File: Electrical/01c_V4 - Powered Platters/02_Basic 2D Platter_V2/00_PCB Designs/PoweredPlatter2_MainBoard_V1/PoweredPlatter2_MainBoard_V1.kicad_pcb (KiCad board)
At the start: 2 copper layers, 60 x 60 mm, 24 parts, among them J1 Conn_01x08, J2 Conn_01x08, J3 M20-7920242R, J4 Conn_01x03, U1 STM32C071KBTx, Y1 16Mhz, 3.2 x 2.5

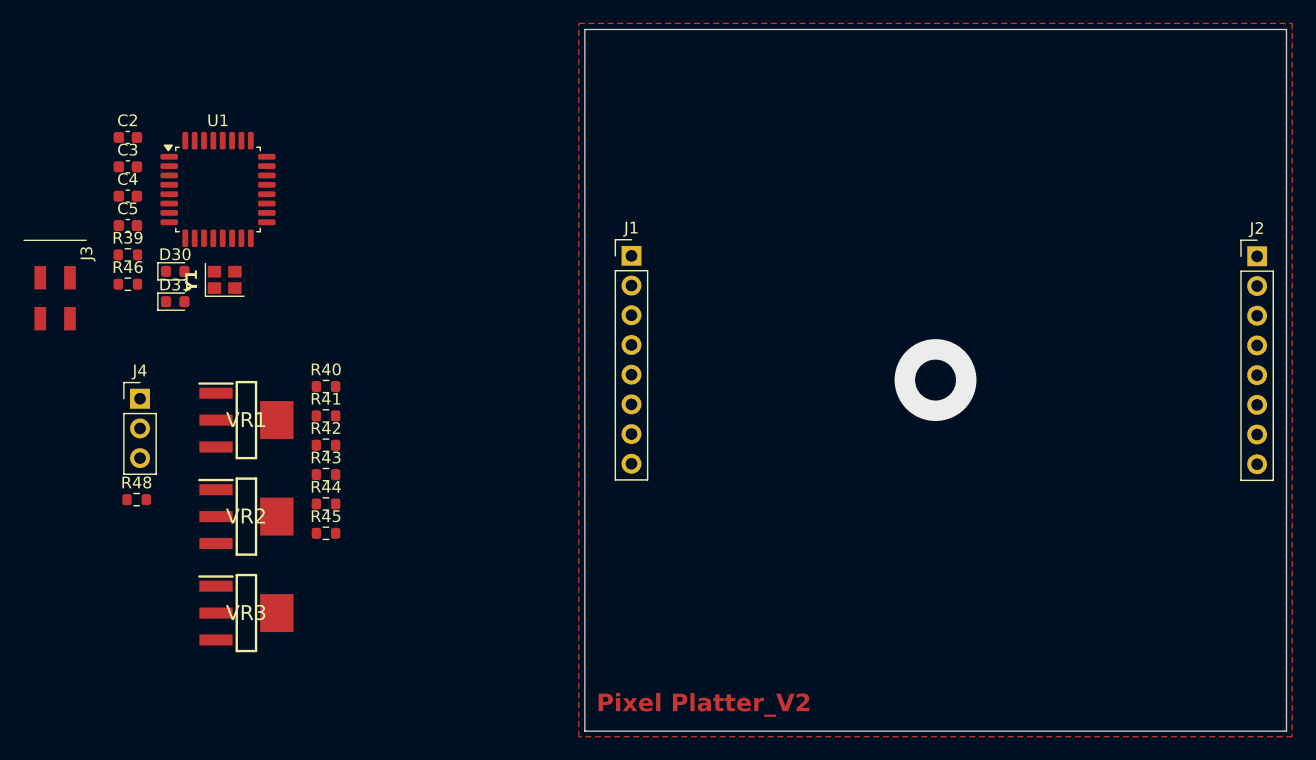
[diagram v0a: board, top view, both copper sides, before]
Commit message: second powered platter main PCB designed and ready for CNC milling
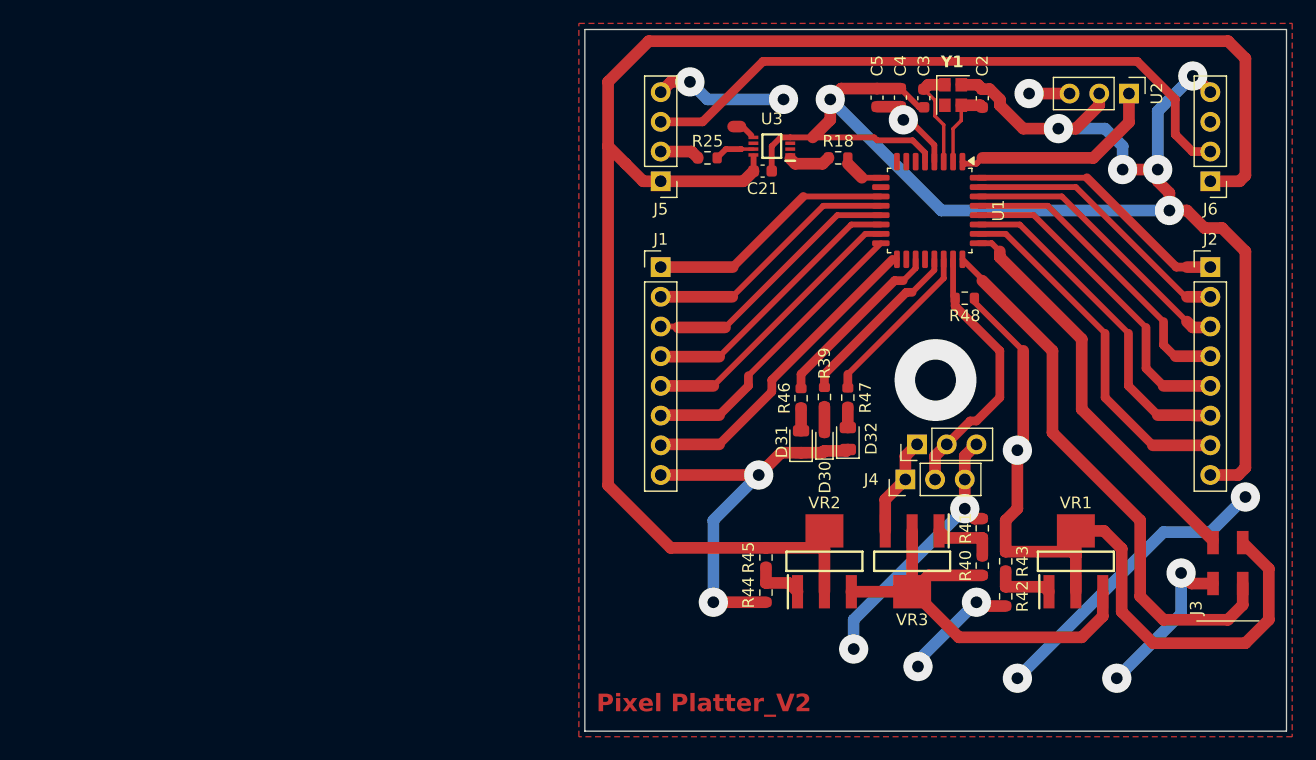
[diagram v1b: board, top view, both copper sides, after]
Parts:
- added C21: 0.1uF_0603, Capacitor_SMD:C_0603_1608Metric, F.Cu at (127.2, 72.1)
- added D32: LED_0805_GREEN, LED_SMD:LED_0805_2012Metric, F.Cu at (134.5, 95.0)
- added J5: Conn_01x04, Connector_PinHeader_2.54mm:PinHeader_1x04_P2.54mm_Vertical, F.Cu at (118.5, 73.0)
- added J5: Conn_01x03, Connector_PinHeader_2.54mm:PinHeader_1x03_P2.54mm_Vertical, F.Cu at (140.4, 95.5)
- added J6: Conn_01x04, Connector_PinHeader_2.54mm:PinHeader_1x04_P2.54mm_Vertical, F.Cu at (165.5, 73.0)
- added R18: 300ohm_0603, Resistor_SMD:R_0603_1608Metric, F.Cu at (133.7, 71.0)
- added R25: 300ohm_0603, Resistor_SMD:R_0603_1608Metric, F.Cu at (122.5, 71.0)
- added R47: 1kohm_0603, Resistor_SMD:R_0603_1608Metric, F.Cu at (134.5, 91.5)
- added U2: IR_Receiver, Connector_PinHeader_2.54mm:PinHeader_1x03_P2.54mm_Vertical, F.Cu at (158.5, 65.5)
- added U3: 74HC3G34DC, PixelPlatter:74HC3G34DC, F.Cu at (128.0, 70.0)
- D31: value LED_0603_BLUE -> LED_0805_RED; footprint LED_SMD:LED_0603_1608Metric -> LED_SMD:LED_0805_2012Metric
- moved J3 106.0 mm to (167.0, 111.5), turned to 180 degrees
- moved C2 73.1 mm to (146.0, 65.9), turned to 90 degrees
- moved R48 72.9 mm to (144.5, 83.0)
- moved VR1 72.0 mm to (154.0, 105.5), turned to 90 degrees
- moved C3 68.3 mm to (141.0, 65.9), turned to 90 degrees
- moved C4 66.6 mm to (139.0, 65.8), turned to 90 degrees
- moved J4 65.8 mm to (139.4, 98.5), turned to 90 degrees
- moved C5 65.0 mm to (137.0, 65.8), turned to 90 degrees
- moved Y1 64.3 mm to (143.5, 65.6), turned to -90 degrees
- moved U1 60.9 mm to (141.5, 75.5), turned to -90 degrees
- moved R39 60.8 mm to (132.5, 91.5), turned to 90 degrees
- moved R42 59.5 mm to (148.0, 108.5), turned to -90 degrees
- moved R43 58.6 mm to (148.0, 105.5), turned to -90 degrees
- moved R46 58.4 mm to (130.5, 91.5), turned to 90 degrees
- moved R40 58.2 mm to (146.0, 105.9), turned to 90 degrees
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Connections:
- J2 pad 1: bladeLED8 -> bladeLED14
- J2 pad 2: bladeLED9 -> bladeLED13
- J2 pad 3: bladeLED10 -> bladeLED12
- J2 pad 5: bladeLED12 -> bladeLED10
- J2 pad 6: bladeLED13 -> bladeLED9
- J2 pad 7: bladeLED14 -> bladeLED8
- U1 pad 1: unconnected-(U1-PB9-Pad1) -> IR_input
- U1 pad 10: bladeLED4 -> unconnected-(U1-PA3-Pad10)
- U1 pad 11: bladeLED5 -> bladeLED1
- U1 pad 12: bladeLED6 -> bladeLED2
- U1 pad 13: bladeLED7 -> bladeLED3
- U1 pad 14: unconnected-(U1-PA7-Pad14) -> bladeLED4
- U1 pad 15: unconnected-(U1-PB0-Pad15) -> bladeLED5
- U1 pad 16: unconnected-(U1-PB1-Pad16) -> bladeLED6
- U1 pad 17: unconnected-(U1-PB2-Pad17) -> bladeLED7
- U1 pad 19: unconnected-(U1-PA9-Pad19) -> testLED2
- U1 pad 21: unconnected-(U1-PA10-Pad21) -> testLED
- U1 pad 22: testLED2 -> testLED3
- U1 pad 23: testLED -> strobe
- U1 pad 7: bladeLED1 -> unconnected-(U1-PA0-Pad7)
- U1 pad 8: bladeLED2 -> unconnected-(U1-PA1-Pad8)
- U1 pad 9: bladeLED3 -> neopixels_3v3
- Y1 pad 2: GND -> unconnected-(Y1-Pad2)
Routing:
- net GND: track 0.00 -> 254.9 mm, vias 1 -> 18
- net +5V: track 0.00 -> 145.6 mm
- net +3V3: track 0.00 -> 121.6 mm, vias 0 -> 3
- net /Connectors/neopixelOutIn: track 0.00 -> 54.1 mm
- net SWDIO: track 0.00 -> 47.1 mm
- net +9V: track 0.00 -> 37.7 mm
- net SWCLK: track 0.00 -> 34.6 mm
- net bladeLED8: track 0.00 -> 30.5 mm
- net bladeLED9: track 0.00 -> 29.2 mm
- net bladeLED10: track 0.00 -> 27.9 mm
- net bladeLED7: track 0.00 -> 27.4 mm
- net bladeLED11: track 0.00 -> 26.4 mm
- net bladeLED6: track 0.00 -> 25.4 mm
- net bladeLED12: track 0.00 -> 24.5 mm
- net bladeLED5: track 0.00 -> 24.2 mm
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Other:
- copper layers 2 -> 4
- board text added: "This PCB is going to be milled on a deskptop CNC only the front copper will be milled Copper layers that are not the front are externally installed wires Each wire copper layer is separated by net, for assembly convenience"
